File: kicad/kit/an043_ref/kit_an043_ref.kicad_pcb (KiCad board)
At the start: 2 copper layers, 50 x 32.9 mm, 5 parts, among them J1 SMA edge launch

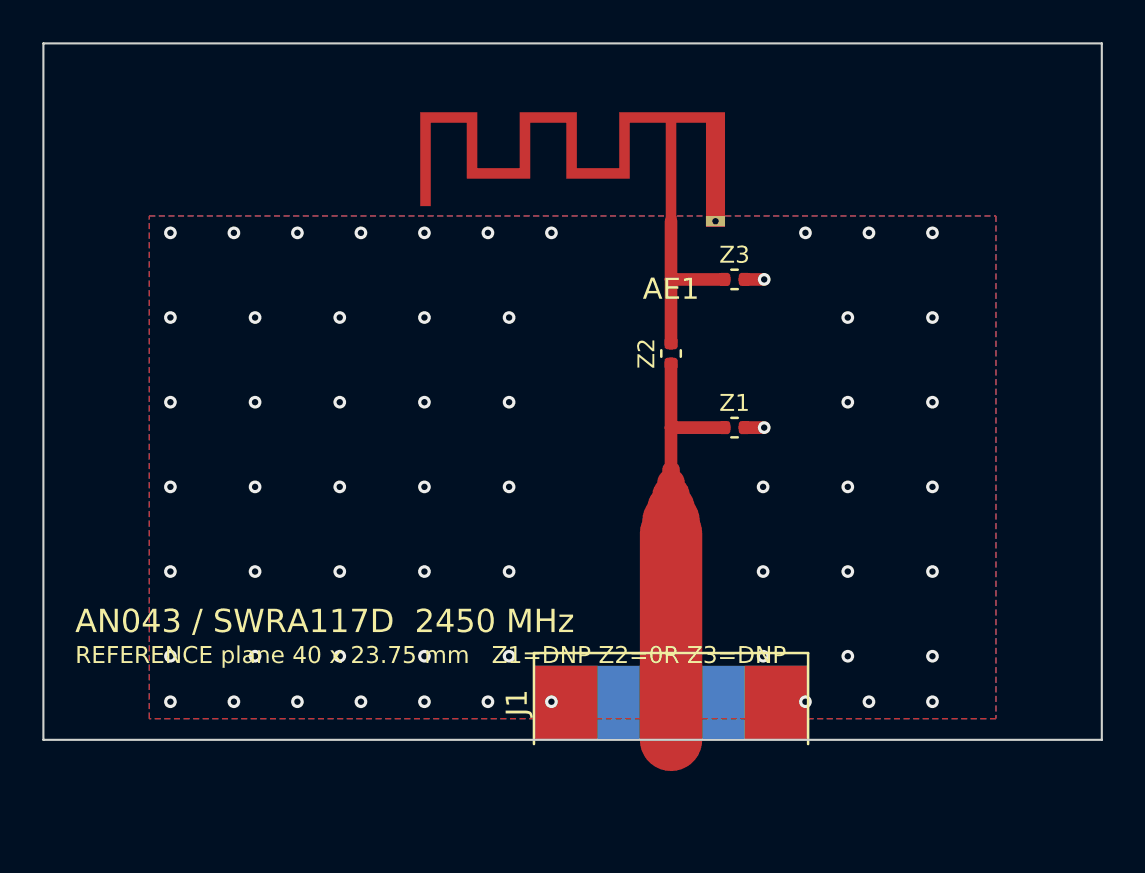
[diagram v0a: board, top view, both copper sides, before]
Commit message: Kit launches through U.FL and a pigtail, not an SMA on the board edge
Embever's own antenna kit feeds its boards through a U.FL and a pigtail
to a bulkhead SMA. That is the better arrangement for a measurement kit
and the kit now does it.

The connector is the smaller half of the reason. The real one is that on
a 45 x 60 mm plane at 868 MHz - lambda 345 mm - the plane and whatever
cable leaves it are one conductor as far as common-mode current goes, so
the braid is part of the antenna and the S11 null moves when the cable
moves. Nothing about the connector fixes that. What U.FL does is let you
fix it: the bulkhead SMA stays on the jig instead of leaving a connector
shell and its ground tabs as copper beside a plane that is half the
antenna, and the pigtail is somewhere to put a ferrite or a sleeve balun,
which is the only real cure. The checklist and the measurement procedure
now both start with choking the cable and proving it by moving it.

The land pattern is Hirose's own for the U.FL-R-SMT-1(10) - signal pad
1.05 x 1.00, ground pads 2.20 x 1.05 - taken from KiCad's
Connector_Coaxial library, which cites Hirose's page for the part. It is
regenerated from those dimensions rather than copied, so the provenance
sits next to the geometry; KiCad's libraries are CC-BY-SA 4.0 with a
design exception and this is the attribution.

A 1.05 mm pad will not take a 2.95 mm line, the same trap the through-
hole SMA sprang with its ground posts. The line tapers 2.95 -> 1.0 mm
over 2.5 mm and runs 1.5 mm into the pad, and the pour keep-away now
stops above the connector so the pour closes around J1's ground pads.
That turns the neck into a grounded coplanar line instead of a
microstrip: line_impedance.py puts 1.0 mm with a 0.2 mm gap at 53.9 ohm
against 84.5 ohm bare, so the neck is near 50 ohm by construction rather
than a lump for the network to absorb.

The launch needed its own rules, because the general ones do not cover
it: a track and the pad it runs to are the same net, s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
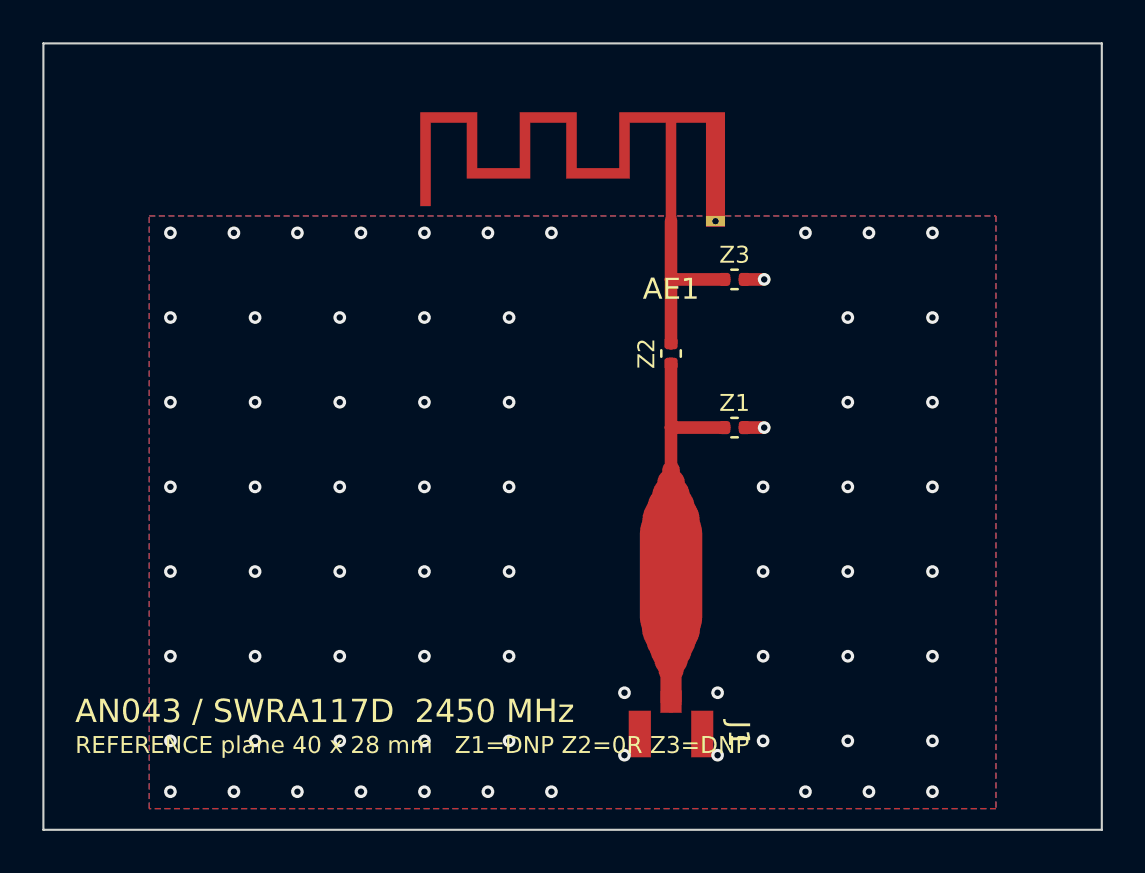
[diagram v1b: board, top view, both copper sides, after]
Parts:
- J1: value SMA edge launch -> U.FL receptacle; footprint SWRA117D_RF:SMA_EdgeMount_Generic -> SWRA117D_RF:U_FL_Hirose_U_FL_R_SMT_1_Vertical
- moved J1 0.75 mm to (129.7, 92.2), turned to 270 degrees
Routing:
- net RF_IN: track 20.3 -> 18.5 mm
- net GND: vias 60 -> 72
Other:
- board size 50 x 32.9 mm -> 50 x 37.2 mm
- board text added: "REFERENCE plane 40 x 28 mm Z1=DNP Z2=0R Z3=DNP"
- board text removed: "REFERENCE plane 40 x 23.75 mm Z1=DNP Z2=0R Z3=DNP"
